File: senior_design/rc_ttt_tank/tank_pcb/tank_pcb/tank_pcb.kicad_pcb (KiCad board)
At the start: 2 copper layers, 85 x 70 mm, 49 parts, among them J1 TURRET, J2 FIRE, J3 DRIVING, J4 FW, J5 PWR, J6 P_TEST, Q1 NMOS, Q2 NMOS, Q3 NMOS, U1 ESP32-DEVKIT-V1

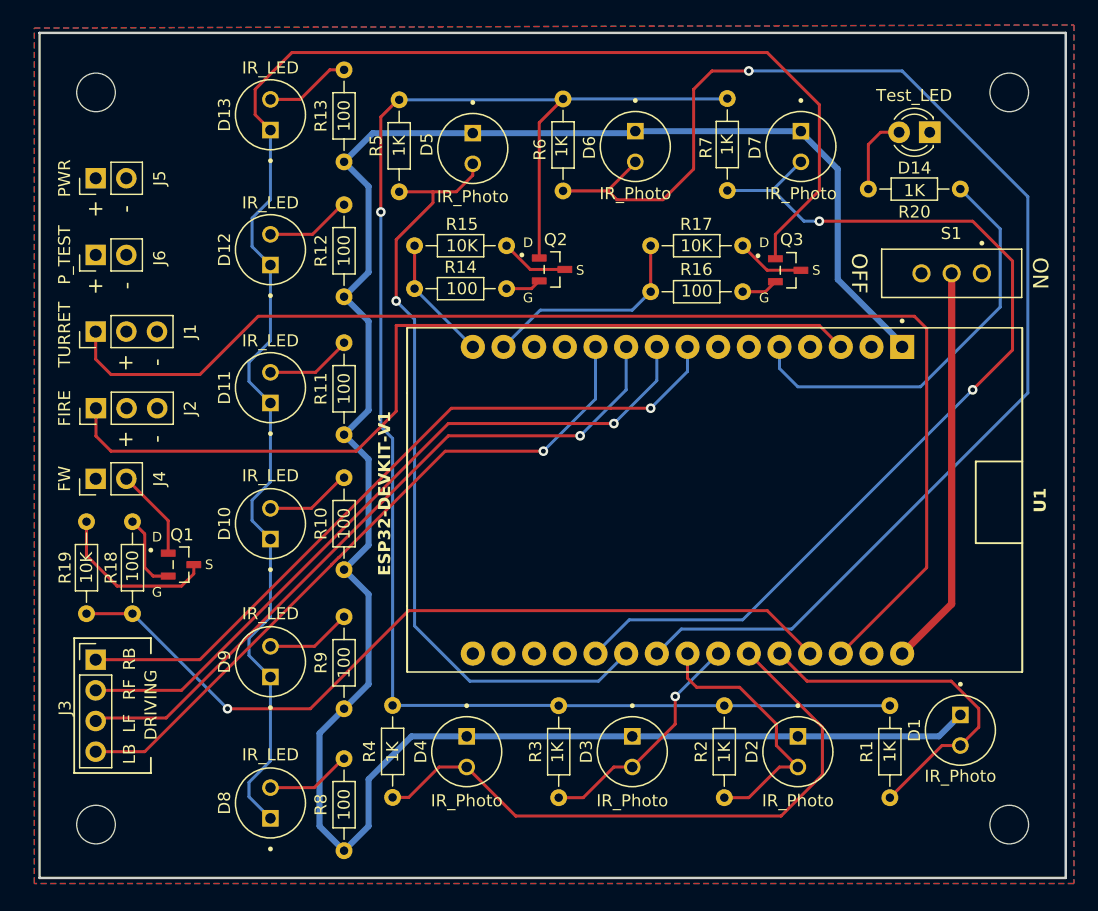
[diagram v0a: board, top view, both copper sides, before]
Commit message: Redesigned my tank pcb. Also got ADC output on sensor 1 and was able to detect IR light!
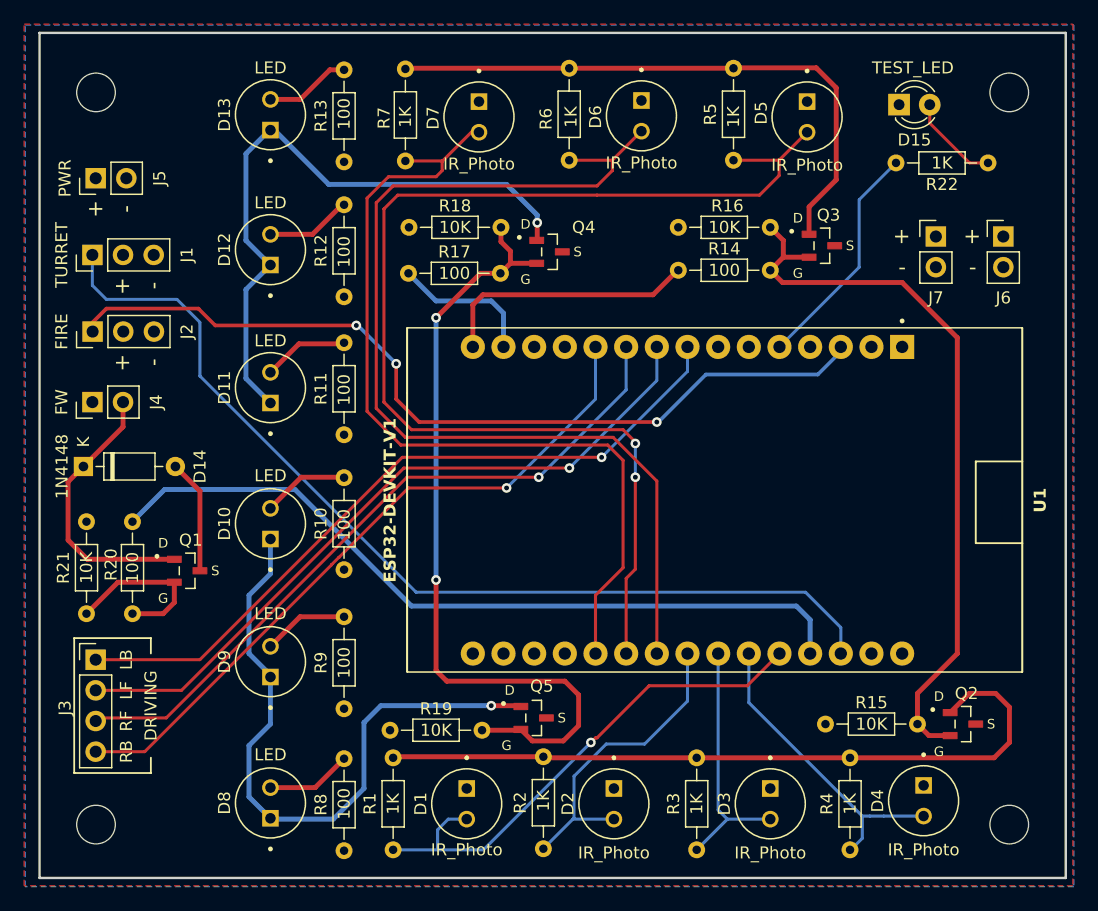
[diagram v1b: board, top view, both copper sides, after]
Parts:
- removed S1: EG1218, library_fp:SW_EG1218
- added D15: TEST_LED, LED_THT:LED_D3.0mm, F.Cu at (171.2, 75.7)
- added J7: TEST_2, Connector_PinHeader_2.54mm:PinHeader_1x02_P2.54mm_Vertical, F.Cu at (174.2, 86.6)
- added Q4: NMOS, 2N7002LT1G:SOT95P240X111-3N, F.Cu at (142.2, 87.9)
- added Q5: NMOS, 2N7002LT1G:SOT95P240X111-3N, F.Cu at (140.9, 126.5)
- added R21: 10K, Resistor_THT:R_Axial_DIN0204_L3.6mm_D1.6mm_P7.62mm_Horizontal, F.Cu at (103.9, 117.9)
- added R22: 1K, Resistor_THT:R_Axial_DIN0204_L3.6mm_D1.6mm_P7.62mm_Horizontal, F.Cu at (170.9, 80.5)
- D10, D11, D12, D13, D8, D9: value IR_LED -> LED
- D14: value Test_LED -> 1N4148; footprint LED_THT:LED_D3.0mm -> Diode_THT:D_DO-35_SOD27_P7.62mm_Horizontal
- J6: value P_TEST -> TEST_1
- R16, R18: value 100 -> 10K
- R17: value 10K -> 100
- R20: value 1K -> 100
- moved D14 75.4 mm to (103.6, 105.7), turned to 0 degrees
- moved J6 75.2 mm to (179.8, 86.6), turned to 0 degrees
- moved R20 73.9 mm to (107.7, 110.2), turned to -90 degrees
- moved Q2 50.8 mm to (176.5, 127.0)
- moved R15 47.6 mm to (165.1, 127.0), turned to 0 degrees
- moved R1 41.4 mm to (129.3, 137.4)
- moved D1 41.3 mm to (135.4, 133.6)
- moved R18 39.4 mm to (130.6, 85.9), turned to 0 degrees
- moved R4 38.1 mm to (167.1, 137.4)
- moved D4 38.1 mm to (173.2, 133.3)
- moved D5 27.8 mm to (163.6, 76.7)
- moved R5 27.8 mm to (157.5, 80.3)
- moved R19 26.9 mm to (129.0, 127.5), turned to 0 degrees
- moved R7 26.8 mm to (130.3, 80.4)
- moved D7 26.8 mm to (136.4, 76.7)
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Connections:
- D1 pad 1: /3.3V -> +3V3
- D11 pad 1: Net-(D10-K) -> Net-(D11-K)
- D12 pad 1: Net-(D10-K) -> Net-(D11-K)
- D13 pad 1: Net-(D10-K) -> Net-(D11-K)
- D14 pad 1: GND -> Net-(D14-K)
- D14 pad 2: Net-(D14-A) -> GND
- D2 pad 1: /3.3V -> +3V3
- D3 pad 1: /3.3V -> +3V3
- D4 pad 1: /3.3V -> +3V3
- D5 pad 1: /3.3V -> +3V3
- D6 pad 1: /3.3V -> +3V3
- D7 pad 1: /3.3V -> +3V3
- J4 pad 2: Net-(J4-Pin_2) -> Net-(D14-K)
- Q1 pad 1: Net-(J4-Pin_2) -> Net-(D14-K)
- Q3 pad 1: Net-(D10-K) -> Net-(Q3-D)
- Q3 pad 2: Net-(Q3-G) -> Net-(Q2-G)
- R10 pad 1: /3.3V -> +3V3
- R11 pad 1: /3.3V -> +3V3
- R12 pad 1: /3.3V -> +3V3
- R13 pad 1: /3.3V -> +3V3
- R15 pad 2: /DET_NMOS -> Net-(Q2-G)
- R16 pad 1: Net-(Q3-G) -> GND
- R16 pad 2: /LED_NMOS -> Net-(Q2-G)
- R17 pad 1: GND -> Net-(Q4-G)
- R18 pad 1: /FW -> GND
- R18 pad 2: Net-(Q1-G) -> Net-(Q4-G)
- R19 pad 1: /FW -> GND
- R19 pad 2: GND -> Net-(Q4-G)
- R20 pad 1: /TEST -> /FW
- R20 pad 2: Net-(D14-A) -> Net-(Q1-G)
- R5 pad 2: Net-(Q2-D) -> Net-(Q3-D)
- R6 pad 2: Net-(Q2-D) -> Net-(Q3-D)
- R7 pad 2: Net-(Q2-D) -> Net-(Q3-D)
- R8 pad 1: /3.3V -> +3V3
- R9 pad 1: /3.3V -> +3V3
- U1 pad 1: /3.3V -> +3V3
- U1 pad 30: Net-(U1-VIN) -> +3V3
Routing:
- net /3.3V: track 183.7 -> 0.00 mm
- net Net-(D10-K): track 131.9 -> 53.6 mm, vias 0 -> 1
- net Net-(Q2-D): track 133.7 -> 60.6 mm, vias 1 -> 0
- net Net-(Q4-G): track 0.00 -> 67.0 mm, vias 0 -> 2
- net Net-(Q2-G): track 2.97 -> 60.9 mm
- net Net-(D11-K): track 0.00 -> 53.1 mm, vias 0 -> 1
- net Net-(Q3-D): track 0.00 -> 49.5 mm
- net Net-(U1-VIN): track 33.2 -> 0.00 mm
- net /IR_S_5: track 65.8 -> 98.2 mm, vias 1 -> 2
- net /IR_S_4: track 52.3 -> 25.7 mm
- net /IR_S_6: track 110.7 -> 85.5 mm, vias 1 -> 0
- net /TURRET: track 103.9 -> 81.0 mm
- net Net-(D14-K): track 0.00 -> 22.8 mm
- net GND: track 25.2 -> 9.48 mm
- net /TEST: track 35.0 -> 19.2 mm
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- added copper zone on B.Cu, net +3V3
- added copper zone on F.Cu, net GND
- removed copper zone on F.Cu, net +3V3
- removed copper zone on B.Cu, net GND
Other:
- board text added: "100"
- board text added: "10K"
- board text added: "1K"
- board text added: "1N4148"
- board text added: "DRIVING"
- board text added: "ESP32-DEVKIT-V1"
- board text added: "FIRE"
- board text added: "FW"
- board text added: "LB"
- board text added: "LF"
- board text added: "PWR"
- board text added: "Q1"
- board text added: "Q2"
- board text added: "Q3"
- board text added: "RB"
- board text added: "RC-TTT Nate Sheffield 2024 Capstone Project"
- board text added: "RF"
- board text added: "TEST_LED"
- board text added: "TURRET"
- board text added: "U1"
